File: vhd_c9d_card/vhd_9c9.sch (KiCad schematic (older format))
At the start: 47 parts, among them IC1 80C49C, IC10 74LS04, IC11 SN751701P, IC12 74HC04, IC2 8255A, IC3 27C256, IC5 74LS30, IC6 74LS30, IC7 74LS27, IC8 74LS32, IC9 74LS02, Q1 PNP (B641), Q2 NPN (D637), Q3 NPN (D637)

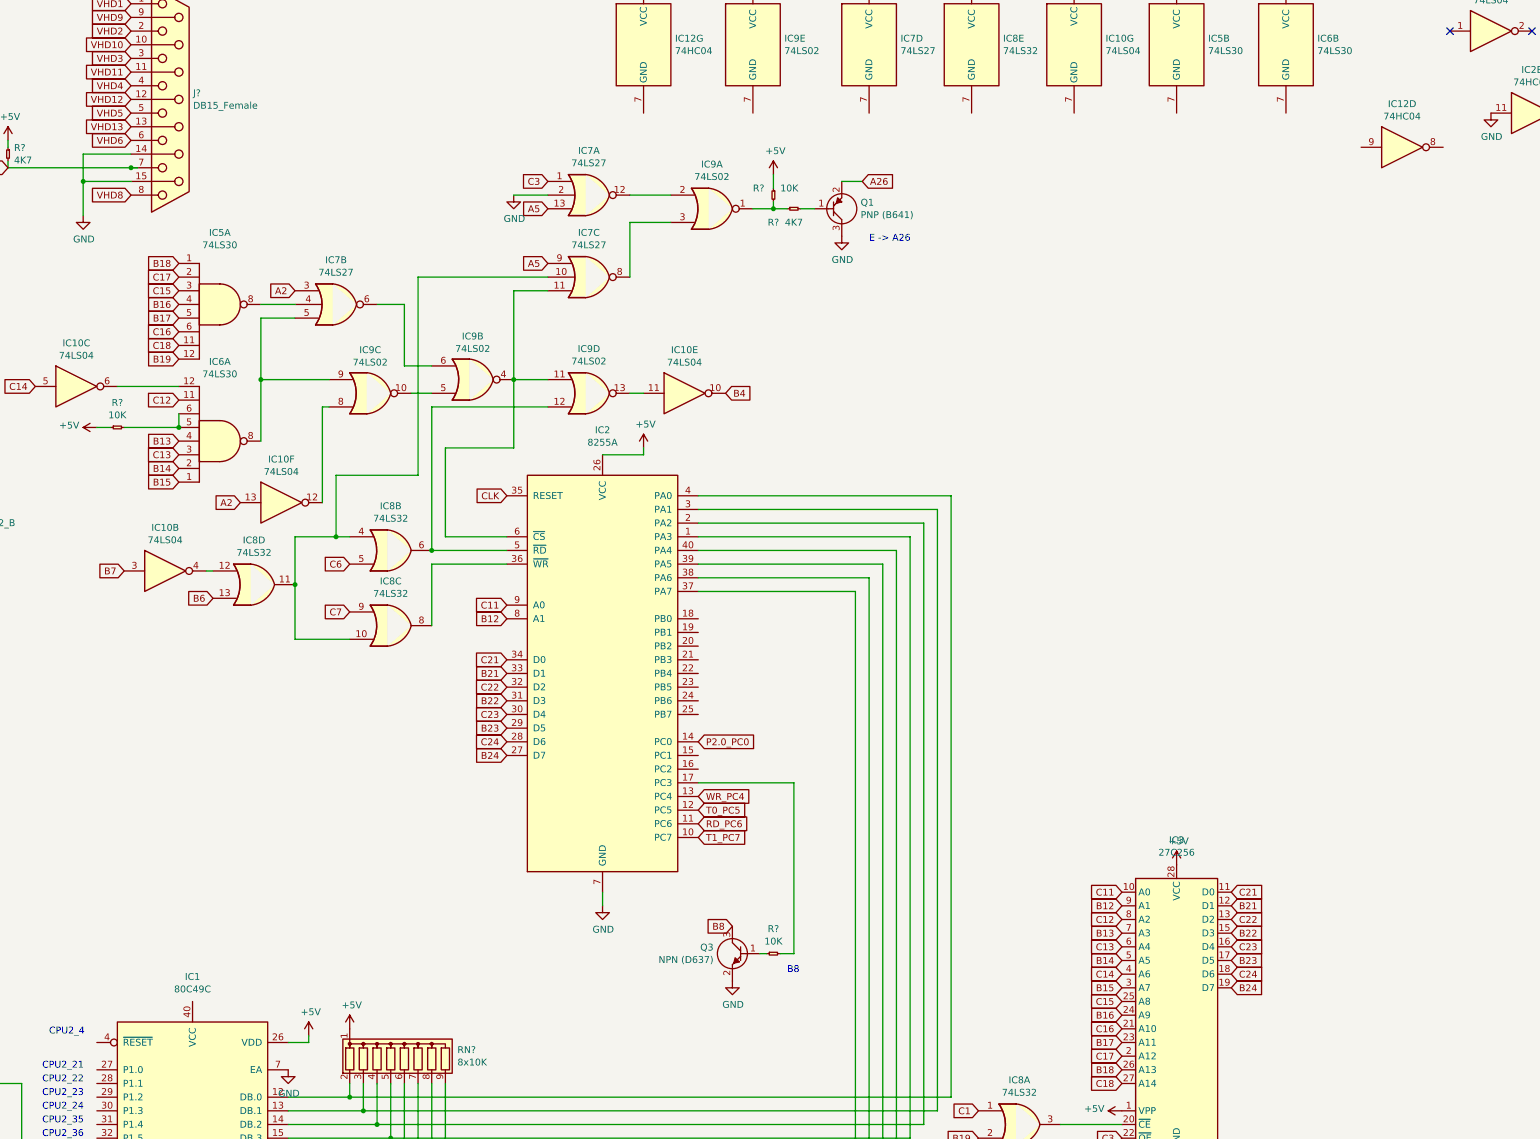
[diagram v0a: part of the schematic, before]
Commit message: Add files via upload
corrected reset signals for 8255 and 80C49C
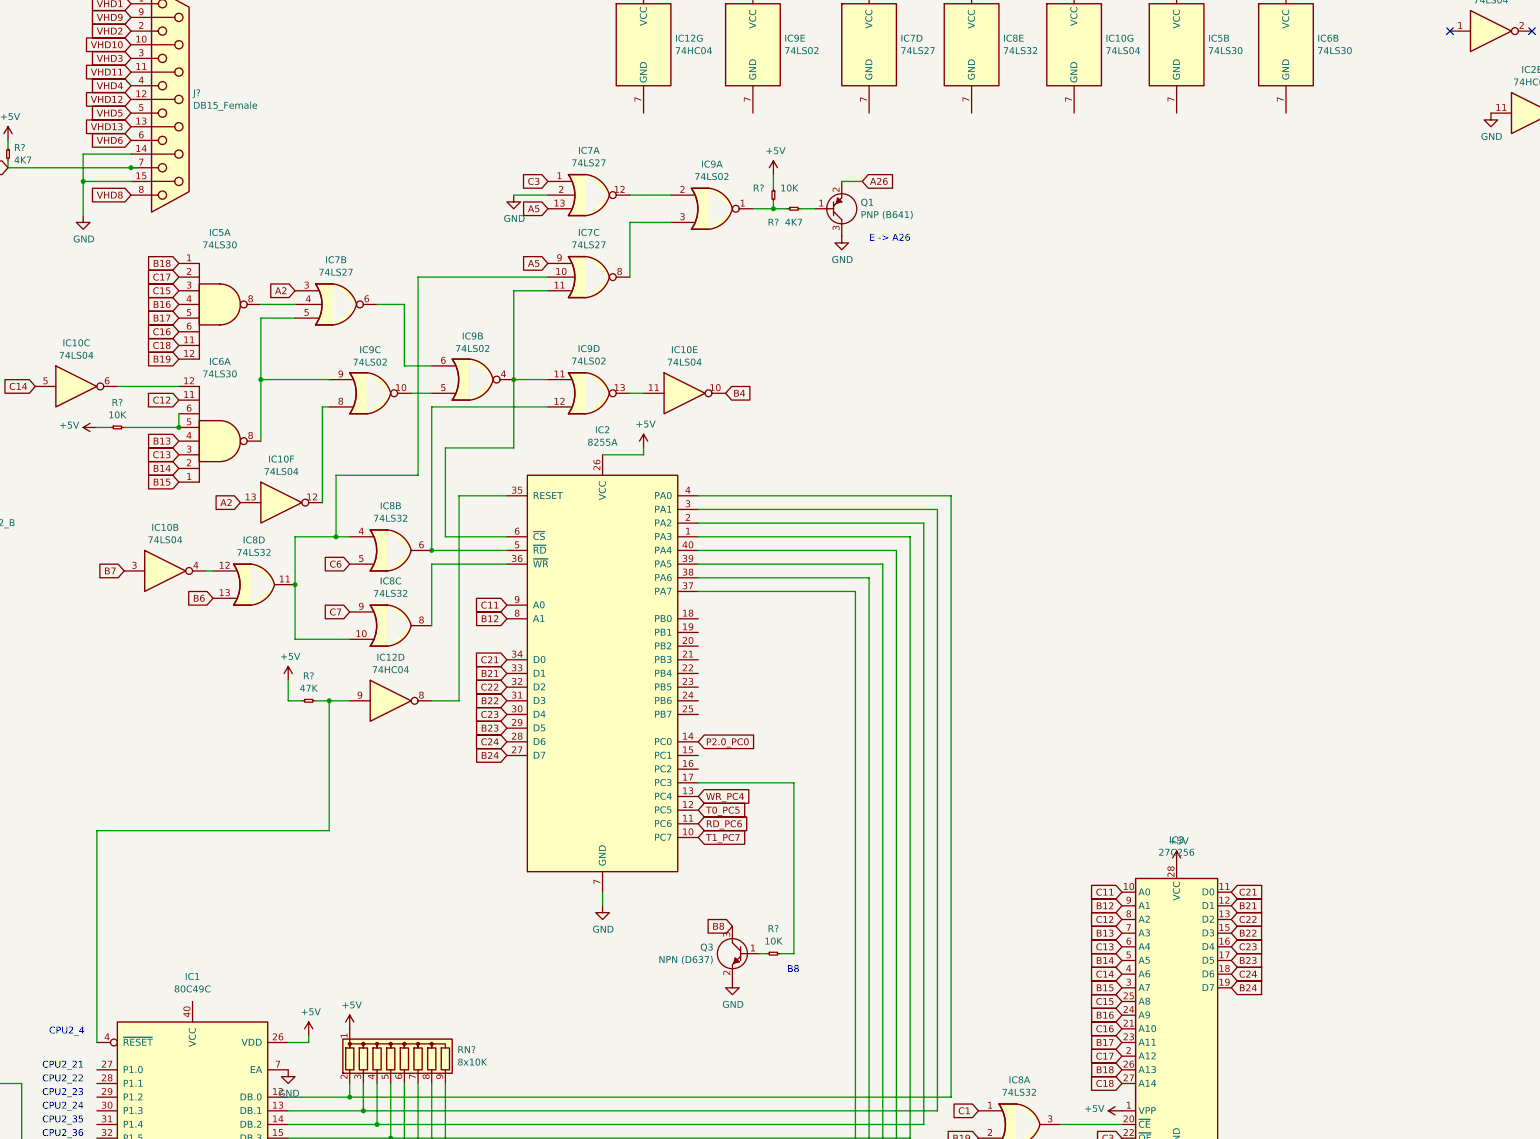
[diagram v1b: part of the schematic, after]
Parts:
- added R?: 47K, symbol agg-kicad:R
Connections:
- net +5V: now also R?.1
- net CLK: no longer IC2.35 (RESET)
- net at IC12.8: now also IC2.35 (RESET)
- net at IC12.9: now also IC1.4 (~RESET~), R?.2
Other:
- moved on the sheet: IC12D
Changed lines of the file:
@@
 L 74xx:74HC04 IC12
 U 4 1 629B3A20
-P 13950 1750
-F 0 "IC12" H 13950 2067 50  0000 C CNN
-F 1 "74HC04" H 13950 1976 50  0000 C CNN
-F 2 "" H 13950 1750 50  0001 C CNN
-F 3 "https://assets.nexperia.com/documents/data-sheet/74HC_HCT04.pdf" H 13950 1750 50  0001 C CNN
-	4    13950 1750
+P 6550 5800
+F 0 "IC12" H 6550 6117 50  0000 C CNN
+F 1 "74HC04" H 6550 6026 50  0000 C CNN
+F 2 "" H 6550 5800 50  0001 C CNN
+F 3 "https://assets.nexperia.com/documents/data-sheet/74HC_HCT04.pdf" H 6550 5800 50  0001 C CNN
+	4    6550 5800
 	1    0    0    -1
 $EndComp
@@
 Text GLabel 6650 10050 0    50   Input ~ 0
 CLK
-Text GLabel 7400 4300 0    50   Input ~ 0
-CLK
+Wire Wire Line
+	7050 4300 7050 5800
+Wire Wire Line
+	7050 5800 6850 5800
+Wire Wire Line
+	7050 4300 7400 4300
+$Comp
+L power:+5V #PWR?
+U 1 1 63A26042
+P 5800 5650
+F 0 "#PWR?" H 5800 5500 50  0001 C CNN
+F 1 "+5V" H 5815 5823 50  0000 C CNN
+F 2 "" H 5800 5650 50  0001 C CNN
+F 3 "" H 5800 5650 50  0001 C CNN
+	1    5800 5650
+	1    0    0    -1
+$EndComp
+$Comp
+L agg-kicad:R R?
+U 1 1 63A274B2
+P 5900 5800
+F 0 "R?" H 5950 5981 50  0000 C CNN
+F 1 "47K" H 5950 5890 50  0000 C CNN
+F 2 "" H 5900 5800 50  0001 C CNN
+F 3 "" H 5900 5800 50  0001 C CNN
+	1    5900 5800
+	1    0    0    -1
+$EndComp
+Wire Wire Line
+	6250 5800 6100 5800
+Wire Wire Line
+	5900 5800 5800 5800
+Wire Wire Line
+	5800 5800 5800 5650
+Wire Wire Line
+	6100 5800 6100 6750
+Wire Wire Line
+	6100 6750 4400 6750
+Wire Wire Line
+	4400 6750 4400 8300
+Connection ~ 6100 5800
+Wire Wire Line
+	6100 5800 6000 5800
 $EndSCHEMATC

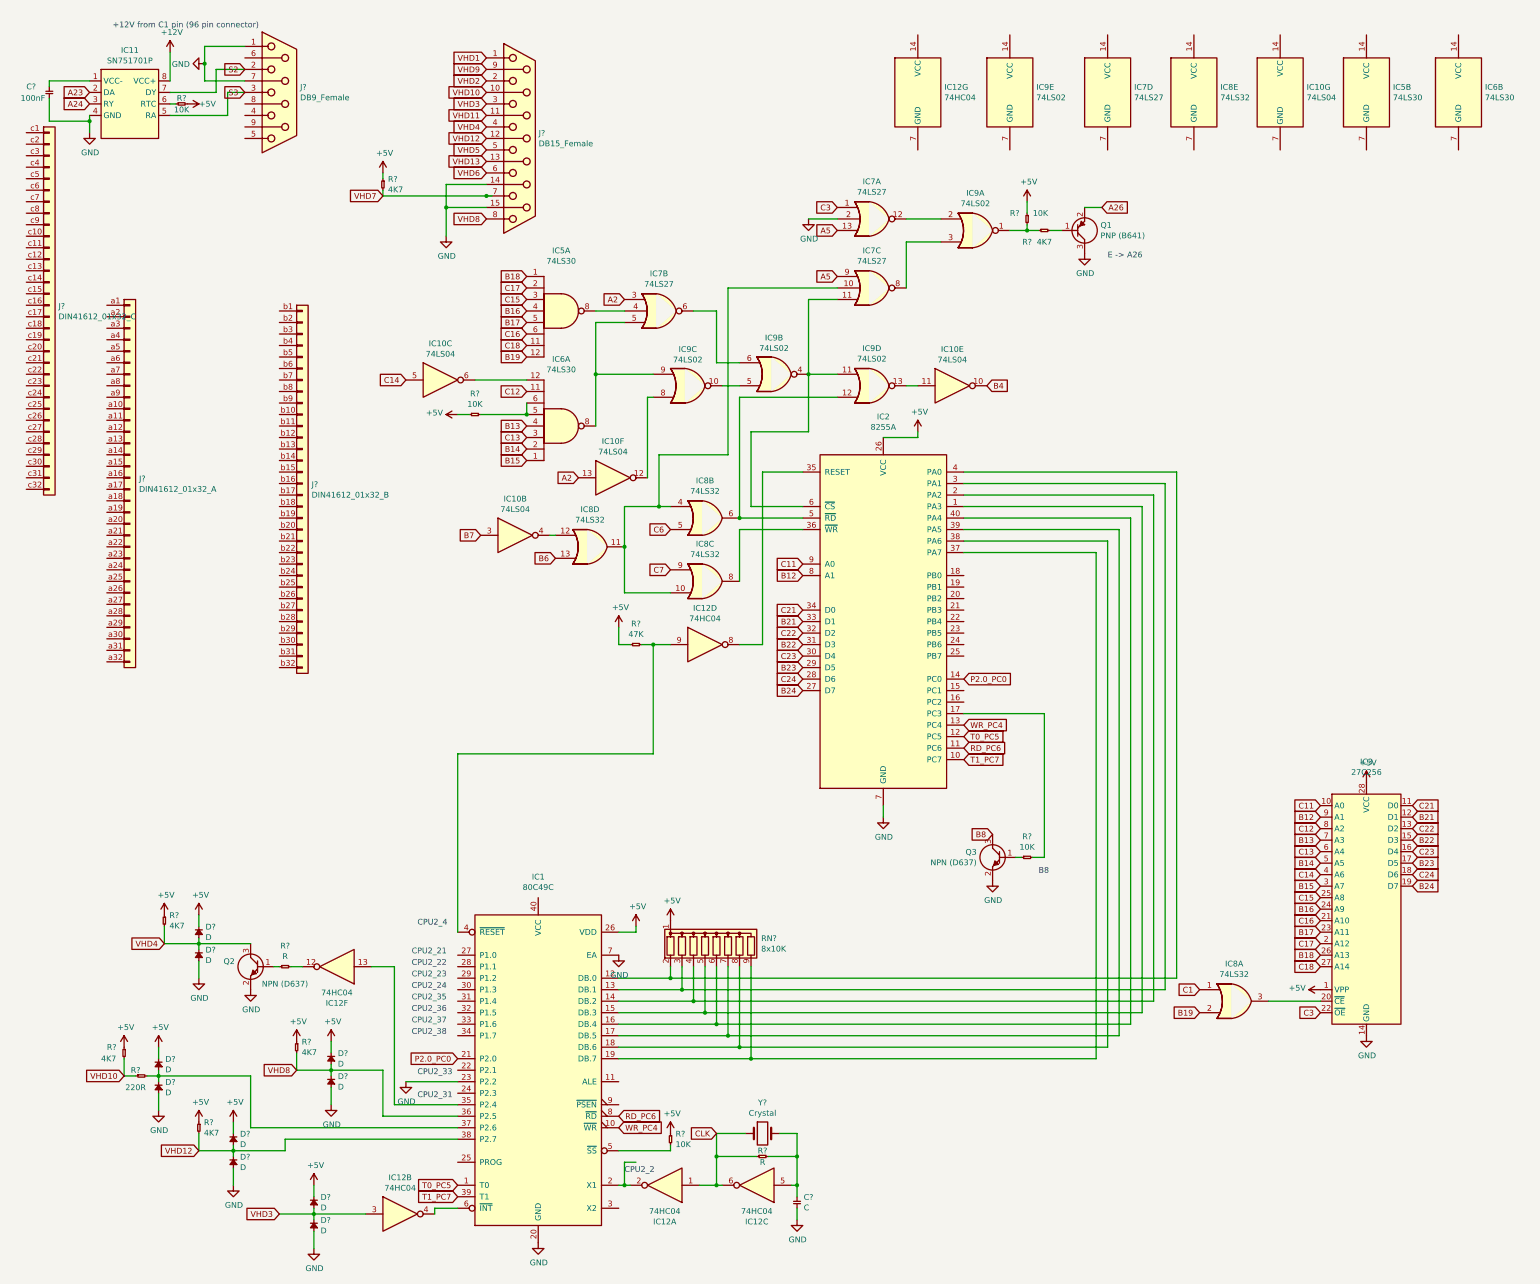
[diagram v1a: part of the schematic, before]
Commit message: added real signal names
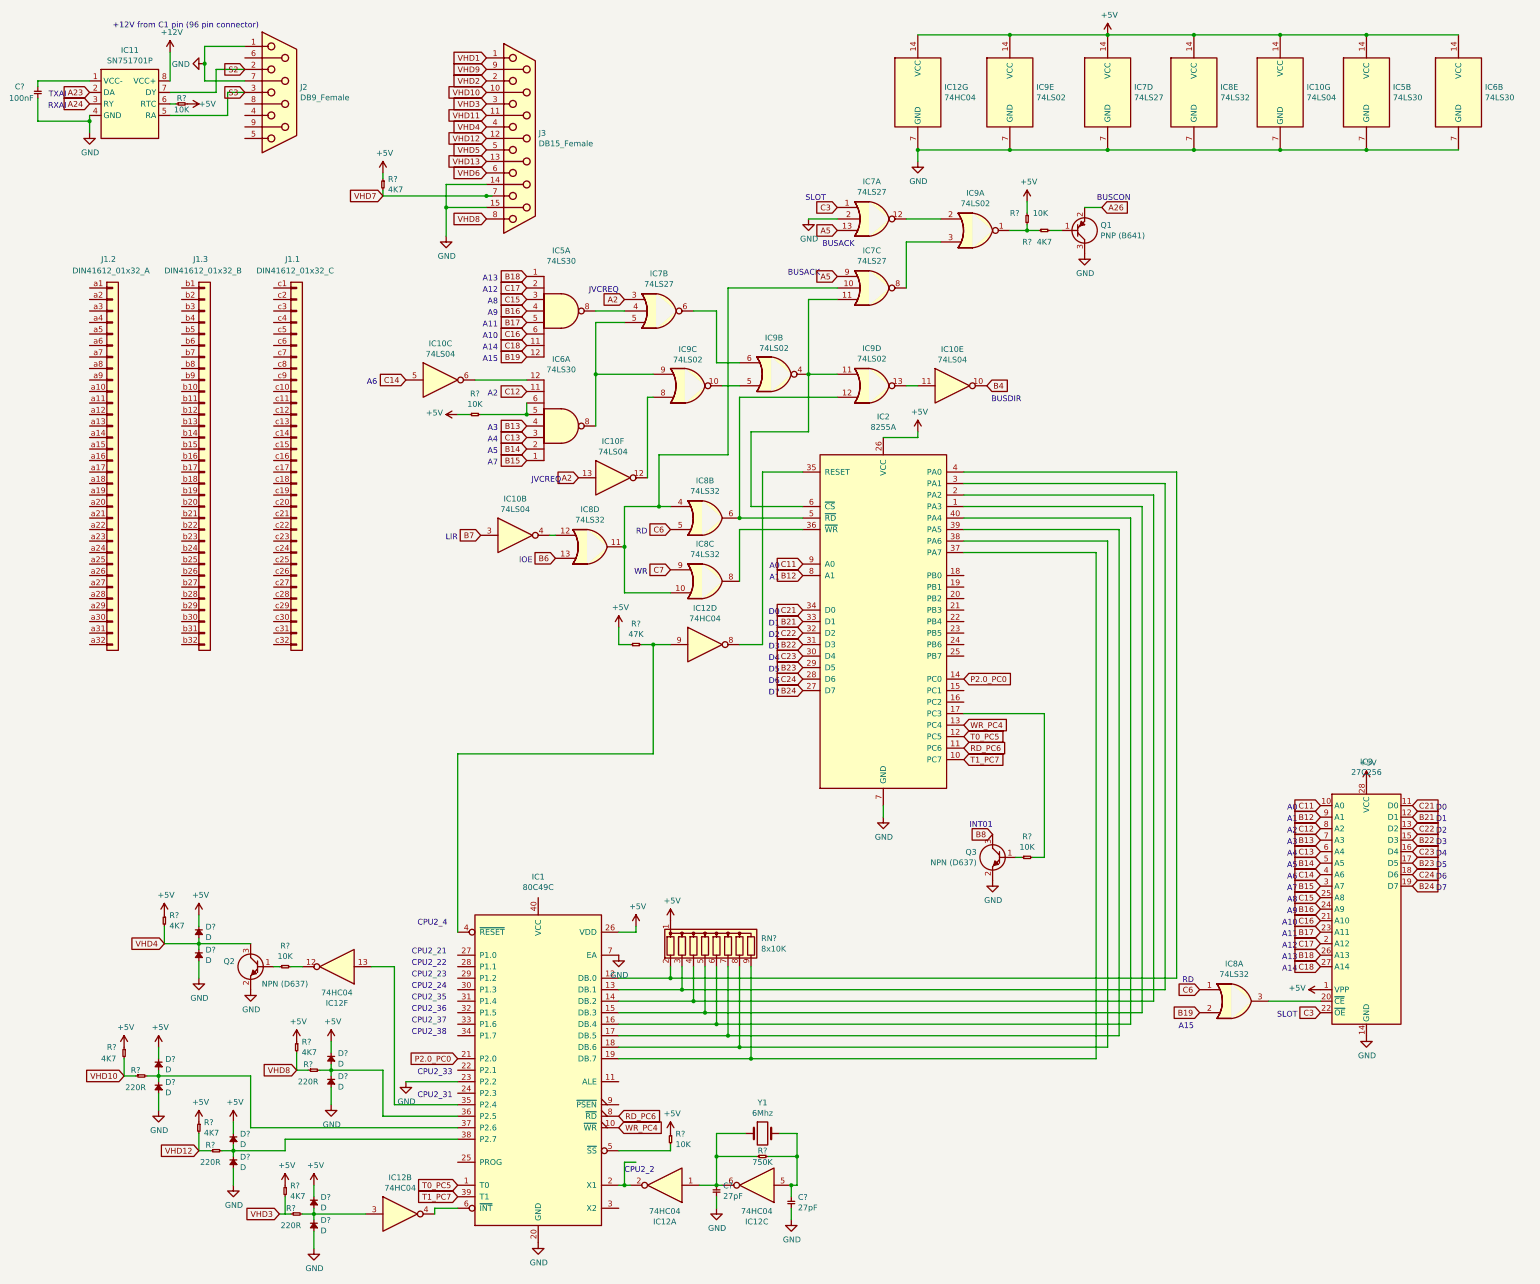
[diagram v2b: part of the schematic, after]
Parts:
- added C?: 27pF, symbol agg-kicad:C
- added R? (x3): 220R, symbol agg-kicad:R
- added R?: 4K7, symbol agg-kicad:R
- C?: value C -> 27pF
- R?: value R -> 750K
- R?: value R -> 10K
- Y1: renamed from Y?; value Crystal -> 6Mhz
- gave numbers to parts that had none: 5
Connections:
- net C1 is gone; now on net C6: IC8.1
- net +5V: now also IC10.14 (VCC), IC12.14 (VCC), IC5.14 (VCC), IC6.14 (VCC), IC7.14 (VCC), IC8.14 (VCC), IC9.14 (VCC), R?.1
- net GND: now also IC10.7 (GND), IC12.7 (GND), IC5.7 (GND), IC6.7 (GND), IC7.7 (GND), IC8.7 (GND), IC9.7 (GND), C?.2
- net VHD12: now also R?.1; no longer D?.1, D?.2, IC1.38 (P2.7)
- net VHD3: now also R?.1; no longer D?.1, D?.2, IC12.3
- net VHD8: now also R?.1; no longer D?.1, D?.2, IC1.36 (P2.5)
- net CLK: no longer names the net of IC12.1, IC12.6, R?.1, Y1.1
- net CLK: now also C?.1
- new net: D?.1, D?.2, IC12.3, R?.2
- new net: D?.1, D?.2, IC1.36 (P2.5), R?.2
- new net: D?.1, D?.2, IC1.38 (P2.7), R?.2
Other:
- note added: "A0"
- note added: "A1"
- note added: "A10"
- note added: "A11"
- note added: "A12"
- note added: "A13"
- note added: "A14"
- note added: "A15"
- note added: "A2"
- note added: "A3"
- note added: "A4"
- note added: "A5"
- note added: "A6"
- note added: "A7"
- note added: "A8"
- note added: "A9"
- note added: "BUSACK"
- note added: "BUSCON"
- note added: "BUSDIR"
- note added: "D0"
- note added: "D1"
- note added: "D2"
- note added: "D3"
- note added: "D4"
- note added: "D5"
- note added: "D6"
- note added: "D7"
- note added: "INT01"
- note added: "JVCREQ"
- note added: "LlR"
- note added: "RD"
- note added: "RXAI"
- note added: "SLOT"
- note added: "TXAI"
- note added: "WR"
- note added: "lOE"
- note removed: "B8"
- note removed: "E -> A26"
- moved on the sheet: C?, J1.1, J1.2, J1.3

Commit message: Add files via upload
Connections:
- net -12V: now reaches C?.1, IC11.1 (VCC-)
- net VHD1: no longer names the net of J3.1
- net VHD11: no longer names the net of J3.11 (P111)
- net VHD13: no longer names the net of J3.13 (P13)
- net VHD2: no longer names the net of J3.2
- net VHD5: no longer names the net of J3.5
- net VHD6: no longer names the net of J3.6
- net VHD7: no longer names the net of J3.7, R?.2
- net VHD9: no longer names the net of J3.9 (P9)
- no-connect marks 4 -> 16
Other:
- note added: "-12V from C2 pin (96 pin connector)"
- note added: "VHD pins 6,7,9 \nconnected to logic\nonly in C9C pcb\n(go to 4069 ic)"
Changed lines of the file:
@@
 encoding utf-8
 Sheet 1 1
-Title ""
+Title "Victor VHD IF-C9D"
 Date ""
 Rev ""
@@
 	1    0    0    -1
 $EndComp
-Text GLabel 4650 700  0    50   Input ~ 0
-VHD1
-Text GLabel 4650 800  0    50   Input ~ 0
-VHD9
-Text GLabel 4650 900  0    50   Input ~ 0
-VHD2
 Text GLabel 4650 1000 0    50   Input ~ 0
 VHD10
 Text GLabel 4650 1100 0    50   Input ~ 0
 VHD3
-Text GLabel 4650 1200 0    50   Input ~ 0
-VHD11
 Text GLabel 4650 1300 0    50   Input ~ 0
 VHD4
 Text GLabel 4650 1400 0    50   Input ~ 0
 VHD12
-Text GLabel 4650 1500 0    50   Input ~ 0
-VHD5
-Text GLabel 4650 1600 0    50   Input ~ 0
-VHD13
-Text GLabel 4650 1700 0    50   Input ~ 0
-VHD6
-Text GLabel 3750 1900 0    50   Input ~ 0
-VHD7
 Text GLabel 4650 2100 0    50   Input ~ 0
 VHD8
@@
 	1    0    0    -1
 $EndComp
-Text GLabel 2550 800  0    50   Input ~ 0
+Text GLabel 2400 800  1    50   Input ~ 0
 S2
-Text GLabel 2550 1000 0    50   Input ~ 0
+Text GLabel 2300 1200 3    50   Input ~ 0
 S3
 Wire Wire Line
@@
 	0    1    1    0
 $EndComp
-Text Notes 1400 450  0    50   ~ 0
+Text Notes 750  1750 0    50   ~ 0
 +12V from C1 pin (96 pin connector)
 Text GLabel 7400 5200 0    50   Input ~ 0
@@
 RXAI
 Wire Wire Line
-	750  900  1200 900
+	750  900  1050 900
 Wire Wire Line
 	750  1250 1200 1250
@@
 	1    0    0    -1
 $EndComp
+Text Notes 750  1850 0    50   ~ 0
+-12V from C2 pin (96 pin connector)
+$Comp
+L power:-12V #PWR?
+U 1 1 63FBF804
+P 1050 900
+F 0 "#PWR?" H 1050 1000 50  0001 C CNN
+F 1 "-12V" H 1065 1073 50  0000 C CNN
+F 2 "" H 1050 900 50  0001 C CNN
+F 3 "" H 1050 900 50  0001 C CNN
+	1    1050 900
+	1    0    0    -1
+$EndComp
+Connection ~ 1050 900
+Wire Wire Line
+	1050 900  1200 900
+NoConn ~ 2550 700
+NoConn ~ 2550 1100
+NoConn ~ 2550 1200
+NoConn ~ 2550 1300
+NoConn ~ 2550 1400
+NoConn ~ 4650 700
+NoConn ~ 4650 900
+NoConn ~ 4650 1500
+NoConn ~ 4650 1600
+NoConn ~ 4650 1200
+NoConn ~ 4650 1700
+NoConn ~ 4650 800
+Text Notes 4250 1400 2    50   ~ 0
+VHD pins 6,7,9 \nconnected to logic\nonly in C9C pcb\n(go to 4069 ic)
 $EndSCHEMATC
